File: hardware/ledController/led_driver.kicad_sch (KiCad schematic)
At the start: 1 part

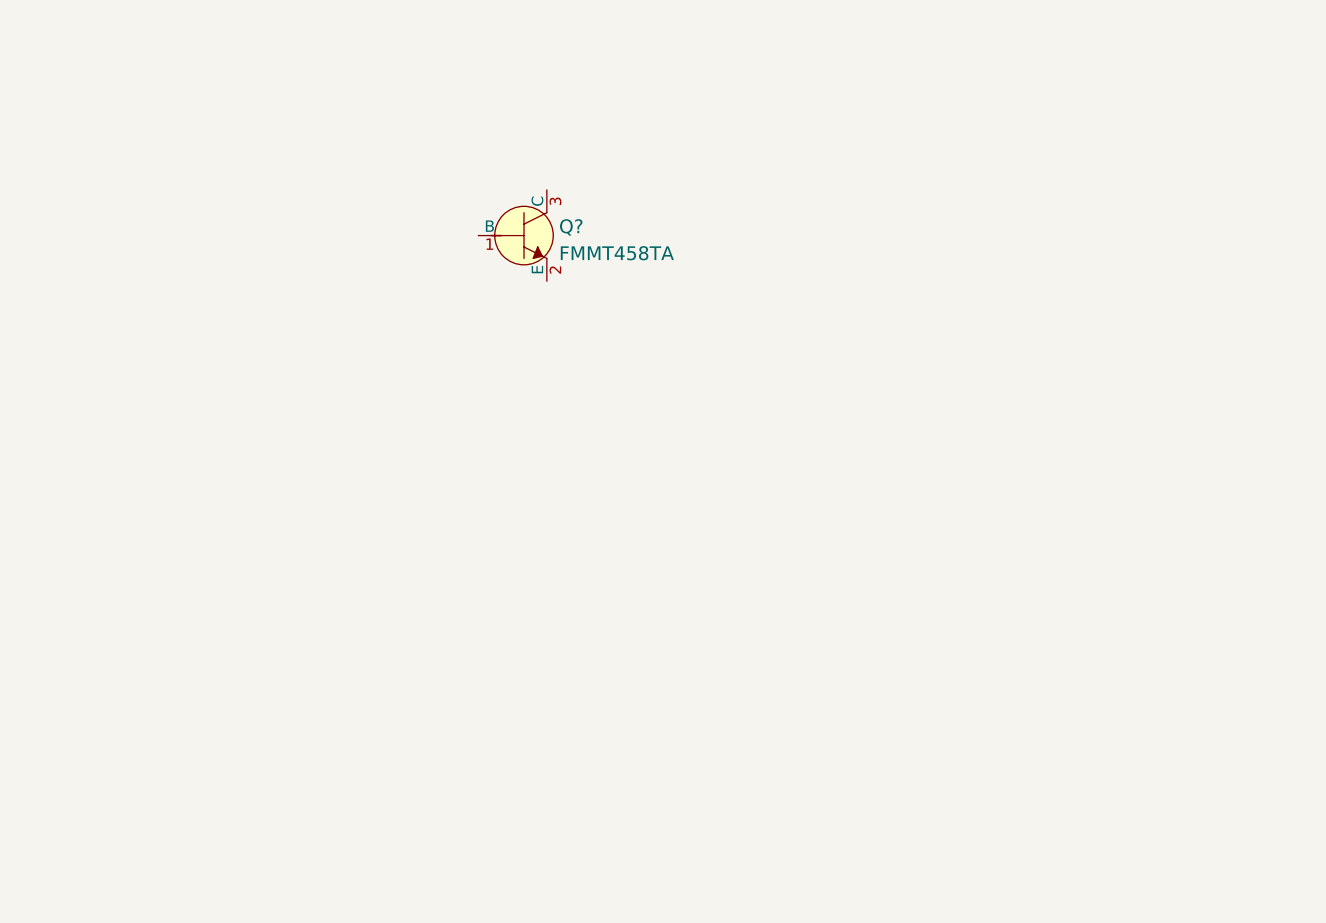
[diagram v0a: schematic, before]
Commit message: Added new schematic page for led current driver
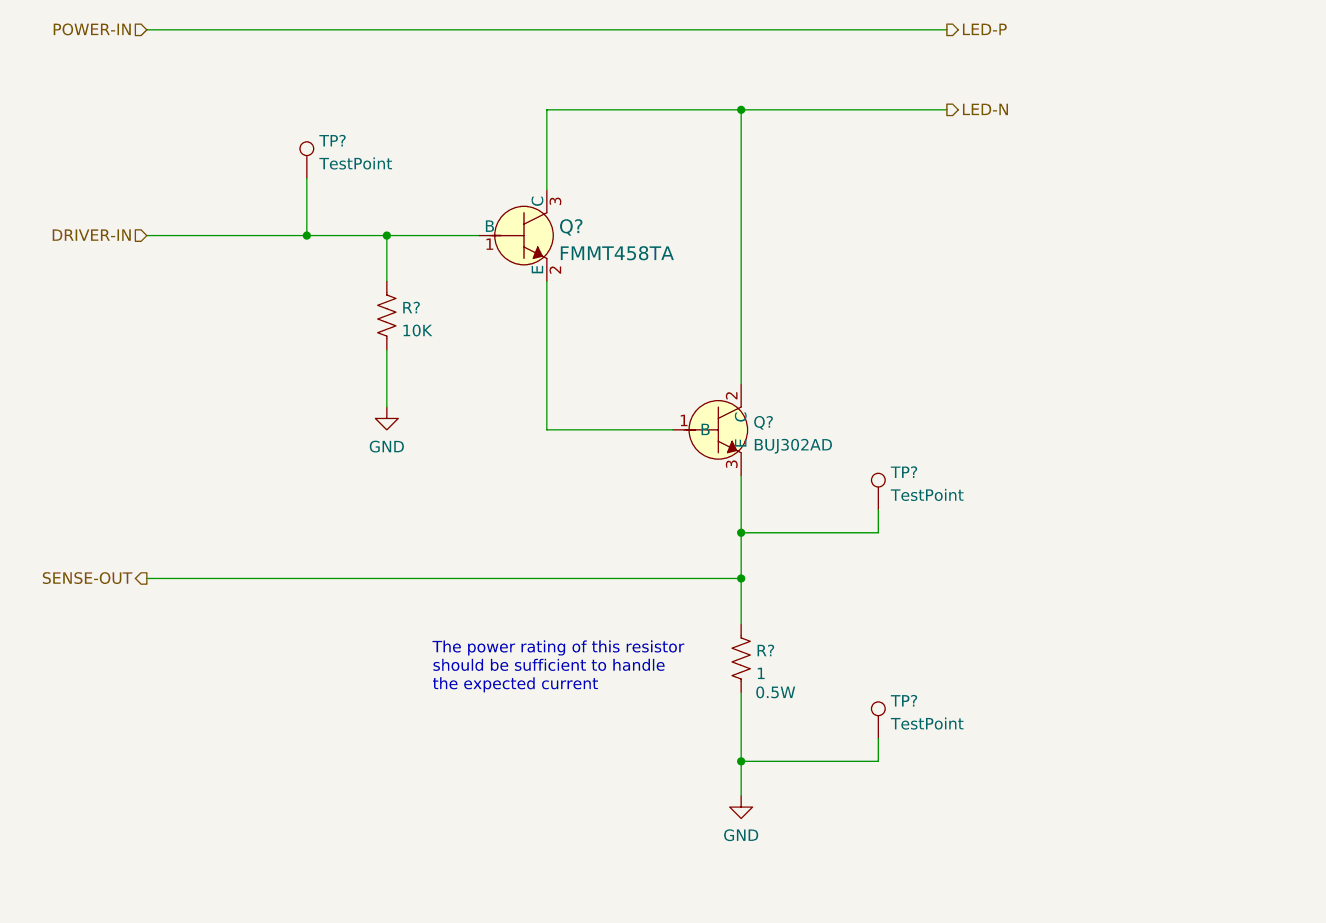
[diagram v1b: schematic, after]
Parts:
- added Q?: BUJ302AD, ym-footprints:SOT-428, symbol ym_BJT:BUJ302AD
- added R?: 10K, Resistor_SMD:R_0402_1005Metric_Pad0.72x0.64mm_HandSolder, symbol Device:R_US
- added R?: 1, Resistor_SMD:R_1210_3225Metric_Pad1.30x2.65mm_HandSolder, symbol Device:R_US
- added TP? (x3): TestPoint, TestPoint:TestPoint_Pad_D1.5mm, symbol Connector:TestPoint
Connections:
- net DRIVER-IN: now reaches Q?.1 (B)
- net DRIVER-IN: now also R?.1, TP?.1
- net at Q?.2 (E): now also Q?.1 (B)
- net LED-N: now reaches Q?.3 (C)
- net LED-N: now also Q?.2 (C)
- new net GND: R?.2, R?.2, TP?.1
- new net SENSE-OUT: Q?.3 (E), R?.1, TP?.1
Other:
- note added: "The power rating of this resistor should be sufficient to handle the expected current"
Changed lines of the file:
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@@
 (kicad_sch (version 20211123) (generator eeschema)
   (paper "A4")
+  (junction (at 102.87 72.39) (diameter 0) (color 0 0 0 0)
+  )
+  (junction (at 142.24 110.49) (diameter 0) (color 0 0 0 0)
+  )
+  (junction (at 142.24 130.81) (diameter 0) (color 0 0 0 0)
+  )
+  (junction (at 142.24 58.42) (diameter 0) (color 0 0 0 0)
+  )
+  (junction (at 93.98 72.39) (diameter 0) (color 0 0 0 0)
+  )
+  (junction (at 142.24 105.41) (diameter 0) (color 0 0 0 0)
+  )
+  (wire (pts (xy 102.87 72.39) (xy 102.87 77.47))
+    (stroke (width 0) (type default) (color 0 0 0 0))
+  )
+  (wire (pts (xy 157.48 128.27) (xy 157.48 130.81))
+    (stroke (width 0) (type default) (color 0 0 0 0))
+  )
+  (wire (pts (xy 142.24 99.06) (xy 142.24 105.41))
+    (stroke (width 0) (type default) (color 0 0 0 0))
+  )
+  (wire (pts (xy 76.2 49.53) (xy 165.1 49.53))
+    (stroke (width 0) (type default) (color 0 0 0 0))
+  )
+  (wire (pts (xy 120.65 93.98) (xy 134.62 93.98))
+    (stroke (width 0) (type default) (color 0 0 0 0))
+  )
+  (wire (pts (xy 76.2 110.49) (xy 142.24 110.49))
+    (stroke (width 0) (type default) (color 0 0 0 0))
+  )
+  (wire (pts (xy 76.2 72.39) (xy 93.98 72.39))
+    (stroke (width 0) (type default) (color 0 0 0 0))
+  )
+  (wire (pts (xy 142.24 130.81) (xy 157.48 130.81))
+    (stroke (width 0) (type default) (color 0 0 0 0))
+  )
+  (wire (pts (xy 157.48 102.87) (xy 157.48 105.41))
+    (stroke (width 0) (type default) (color 0 0 0 0))
+  )
+  (wire (pts (xy 142.24 58.42) (xy 142.24 88.9))
+    (stroke (width 0) (type default) (color 0 0 0 0))
+  )
+  (wire (pts (xy 113.03 72.39) (xy 102.87 72.39))
+    (stroke (width 0) (type default) (color 0 0 0 0))
+  )
+  (wire (pts (xy 142.24 58.42) (xy 165.1 58.42))
+    (stroke (width 0) (type default) (color 0 0 0 0))
+  )
+  (wire (pts (xy 120.65 67.31) (xy 120.65 58.42))
+    (stroke (width 0) (type default) (color 0 0 0 0))
+  )
+  (wire (pts (xy 102.87 85.09) (xy 102.87 91.44))
+    (stroke (width 0) (type default) (color 0 0 0 0))
+  )
+  (wire (pts (xy 120.65 58.42) (xy 142.24 58.42))
+    (stroke (width 0) (type default) (color 0 0 0 0))
+  )
+  (wire (pts (xy 93.98 66.04) (xy 93.98 72.39))
+    (stroke (width 0) (type default) (color 0 0 0 0))
+  )
+  (wire (pts (xy 142.24 105.41) (xy 142.24 110.49))
+    (stroke (width 0) (type default) (color 0 0 0 0))
+  )
+  (wire (pts (xy 142.24 105.41) (xy 157.48 105.41))
+    (stroke (width 0) (type default) (color 0 0 0 0))
+  )
+  (wire (pts (xy 120.65 77.47) (xy 120.65 93.98))
+    (stroke (width 0) (type default) (color 0 0 0 0))
+  )
+  (wire (pts (xy 142.24 123.19) (xy 142.24 130.81))
+    (stroke (width 0) (type default) (color 0 0 0 0))
+  )
+  (wire (pts (xy 142.24 130.81) (xy 142.24 134.62))
+    (stroke (width 0) (type default) (color 0 0 0 0))
+  )
+  (wire (pts (xy 93.98 72.39) (xy 102.87 72.39))
+    (stroke (width 0) (type default) (color 0 0 0 0))
+  )
+  (wire (pts (xy 142.24 110.49) (xy 142.24 115.57))
+    (stroke (width 0) (type default) (color 0 0 0 0))
+  )
+  (text "The power rating of this resistor\nshould be sufficient to handle\nthe expected current"
+    (at 107.95 123.19 0)
+    (effects (font (size 1.27 1.27)) (justify left bottom))
+  )
+  (hierarchical_label "SENSE-OUT" (shape output) (at 76.2 110.49 180)
+    (effects (font (size 1.27 1.27)) (justify right))
+  )
+  (hierarchical_label "LED-P" (shape output) (at 165.1 49.53 0)
+    (effects (font (size 1.27 1.27)) (justify left))
+  )
+  (hierarchical_label "POWER-IN" (shape input) (at 76.2 49.53 180)
+    (effects (font (size 1.27 1.27)) (justify right))
+  )
+  (hierarchical_label "LED-N" (shape output) (at 165.1 58.42 0)
+    (effects (font (size 1.27 1.27)) (justify left))
+  )
+  (hierarchical_label "DRIVER-IN" (shape input) (at 76.2 72.39 180)
+    (effects (font (size 1.27 1.27)) (justify right))
+  )
   (symbol (lib_id "dk_Transistors-Bipolar-BJT-Single:FMMT458TA") (at 118.11 72.39 0) (unit 1)
     (in_bom yes) (on_board yes) (fields_autoplaced)
@@
     (pin "3")
   )
+  (symbol (lib_id "Connector:TestPoint") (at 157.48 128.27 0) (unit 1)
+    (in_bom yes) (on_board yes) (fields_autoplaced)
+    (property "Reference" "TP?" (id 0) (at 158.877 124.1333 0)
+      (effects (font (size 1.27 1.27)) (justify left))
+    )
+    (property "Value" "TestPoint" (id 1) (at 158.877 126.6702 0)
+      (effects (font (size 1.27 1.27)) (justify left))
+    )
+    (property "Footprint" "TestPoint:TestPoint_Pad_D1.5mm" (id 2) (at 162.56 128.27 0)
+      (effects (font (size 1.27 1.27)) hide)
+    )
+    (property "Datasheet" "~" (id 3) (at 162.56 128.27 0)
+      (effects (font (size 1.27 1.27)) hide)
+    )
+    (pin "1")
+  )
+  (symbol (lib_id "power:GND") (at 142.24 134.62 0) (unit 1)
+    (in_bom yes) (on_board yes) (fields_autoplaced)
+    (property "Reference" "#PWR?" (id 0) (at 142.24 140.97 0)
+      (effects (font (size 1.27 1.27)) hide)
+    )
+    (property "Value" "GND" (id 1) (at 142.24 139.0634 0))
+    (property "Footprint" "" (id 2) (at 142.24 134.62 0)
+      (effects (font (size 1.27 1.27)) hide)
+    )
+    (property "Datasheet" "" (id 3) (at 142.24 134.62 0)
+      (effects (font (size 1.27 1.27)) hide)
+    )
+    (pin "1")
+  )
+  (symbol (lib_id "Connector:TestPoint") (at 93.98 66.04 0) (unit 1)
+    (in_bom yes) (on_board yes) (fields_autoplaced)
+    (property "Reference" "TP?" (id 0) (at 95.377 61.9033 0)
+      (effects (font (size 1.27 1.27)) (justify left))
+    )
+    (property "Value" "TestPoint" (id 1) (at 95.377 64.4402 0)
+      (effects (font (size 1.27 1.27)) (justify left))
+    )
+    (property "Footprint" "TestPoint:TestPoint_Pad_D1.5mm" (id 2) (at 99.06 66.04 0)
+      (effects (font (size 1.27 1.27)) hide)
+    )
+    (property "Datasheet" "~" (id 3) (at 99.06 66.04 0)
+      (effects (font (size 1.27 1.27)) hide)
+    )
+    (pin "1")
+  )
+  (symbol (lib_id "Device:R_US") (at 102.87 81.28 0) (unit 1)
+    (in_bom yes) (on_board yes) (fields_autoplaced)
+    (property "Reference" "R?" (id 0) (at 104.521 80.4453 0)
+      (effects (font (size 1.27 1.27)) (justify left))
+    )
+    (property "Value" "10K" (id 1) (at 104.521 82.9822 0)
+      (effects (font (size 1.27 1.27)) (justify left))
+    )
+    (property "Footprint" "Resistor_SMD:R_0402_1005Metric_Pad0.72x0.64mm_HandSolder" (id 2) (at 103.886 81.534 90)
+      (effects (font (size 1.27 1.27)) hide)
+    )
+    (property "Datasheet" "~" (id 3) (at 102.87 81.28 0)
+      (effects (font (size 1.27 1.27)) hide)
+    )
+    (pin "1")
+    (pin "2")
+  )
+  (symbol (lib_id "Device:R_US") (at 142.24 119.38 0) (unit 1)
+    (in_bom yes) (on_board yes)
+    (property "Reference" "R?" (id 0) (at 143.891 118.5453 0)
+      (effects (font (size 1.27 1.27)) (justify left))
+    )
+    (property "Value" "1" (id 1) (at 143.891 121.0822 0)
+      (effects (font (size 1.27 1.27)) (justify left))
+    )
+    (property "Footprint" "Resistor_SMD:R_1210_3225Metric_Pad1.30x2.65mm_HandSolder" (id 2) (at 143.256 119.634 90)
+      (effects (font (size 1.27 1.27)) hide)
+    )
+    (property "Datasheet" "~" (id 3) (at 142.24 119.38 0)
+      (effects (font (size 1.27 1.27)) hide)
+    )
+    (property "Power" "0.5W" (id 4) (at 146.05 123.19 0))
+    (pin "1")
+    (pin "2")
+  )
+  (symbol (lib_id "ym_BJT:BUJ302AD") (at 139.7 93.98 0) (unit 1)
+    (in_bom yes) (on_board yes) (fields_autoplaced)
+    (property "Reference" "Q?" (id 0) (at 143.5862 93.1453 0)
+      (effects (font (size 1.27 1.27)) (justify left))
+    )
+    (property "Value" "BUJ302AD" (id 1) (at 143.5862 95.6822 0)
+      (effects (font (size 1.27 1.27)) (justify left))
+    )
+    (property "Footprint" "ym-footprints:SOT-428" (id 2) (at 139.7 93.98 0)
+      (effects (font (size 1.27 1.27)) hide)
+    )
+    (property "Datasheet" "https://www.ween-semi.com/sites/default/files/2018-11/BUJ302AD.pdf" (id 3) (at 139.7 93.98 0)
+      (effects (font (size 1.27 1.27)) hide)
+    )
+    (pin "1")
+    (pin "2")
+    (pin "3")
+  )
+  (symbol (lib_id "Connector:TestPoint") (at 157.48 102.87 0) (unit 1)
+    (in_bom yes) (on_board yes) (fields_autoplaced)
+    (property "Reference" "TP?" (id 0) (at 158.877 98.7333 0)
+      (effects (font (size 1.27 1.27)) (justify left))
+    )
+    (property "Value" "TestPoint" (id 1) (at 158.877 101.2702 0)
+      (effects (font (size 1.27 1.27)) (justify left))
+    )
+    (property "Footprint" "TestPoint:TestPoint_Pad_D1.5mm" (id 2) (at 162.56 102.87 0)
+      (effects (font (size 1.27 1.27)) hide)
+    )
+    (property "Datasheet" "~" (id 3) (at 162.56 102.87 0)
+      (effects (font (size 1.27 1.27)) hide)
+    )
+    (pin "1")
+  )
+  (symbol (lib_id "power:GND") (at 102.87 91.44 0) (unit 1)
+    (in_bom yes) (on_board yes) (fields_autoplaced)
+    (property "Reference" "#PWR?" (id 0) (at 102.87 97.79 0)
+      (effects (font (size 1.27 1.27)) hide)
+    )
+    (property "Value" "GND" (id 1) (at 102.87 95.8834 0))
+    (property "Footprint" "" (id 2) (at 102.87 91.44 0)
+      (effects (font (size 1.27 1.27)) hide)
+    )
+    (property "Datasheet" "" (id 3) (at 102.87 91.44 0)
+      (effects (font (size 1.27 1.27)) hide)
+    )
+    (pin "1")
+  )
 )

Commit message: Added BJT base resistor and some cleanup
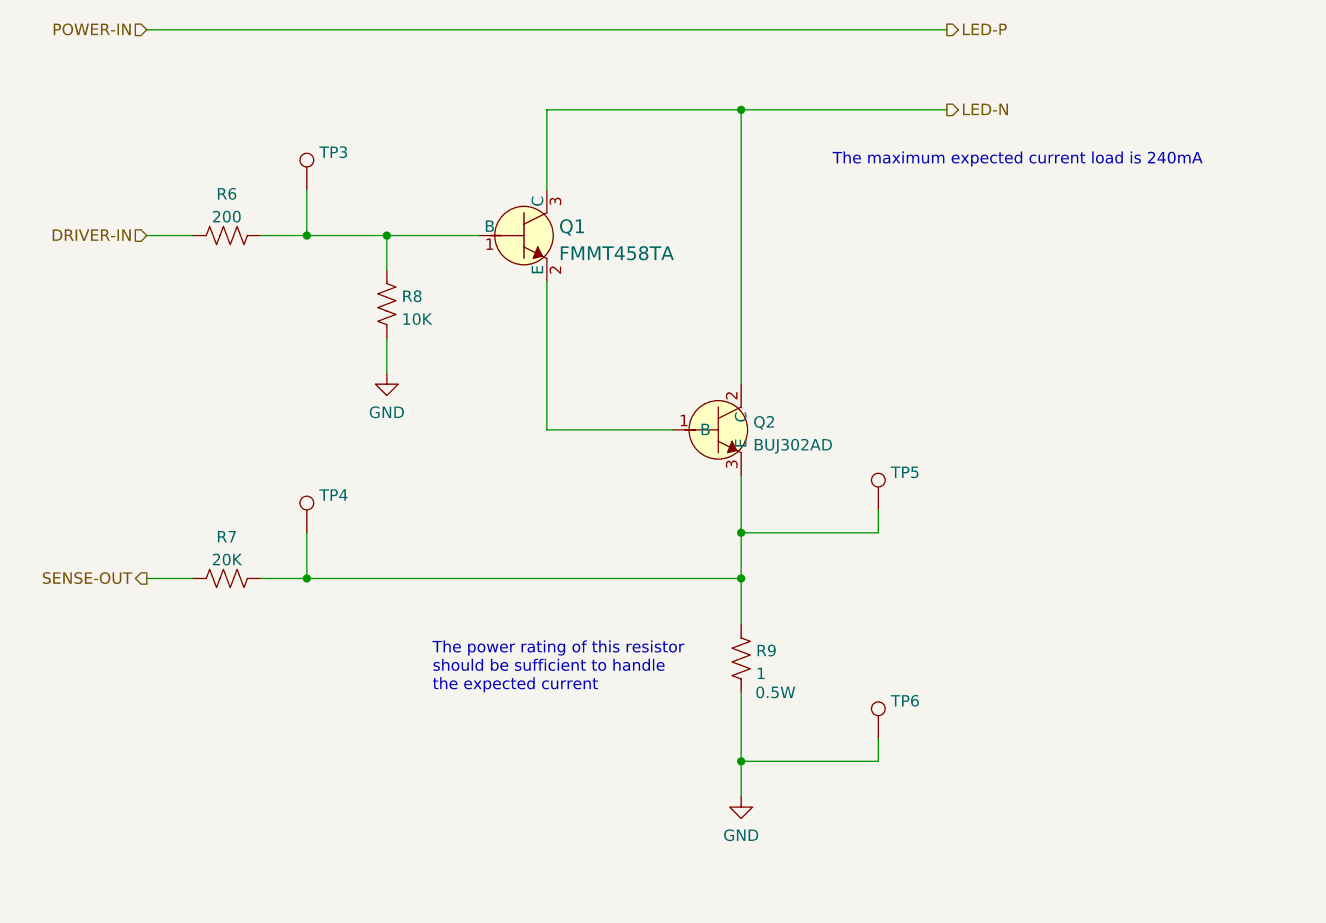
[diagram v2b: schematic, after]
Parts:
- added R6: 200, Resistor_SMD:R_0603_1608Metric_Pad0.98x0.95mm_HandSolder, symbol Device:R_US
- added R7: 20K, Resistor_SMD:R_0603_1608Metric_Pad0.98x0.95mm_HandSolder, symbol Device:R_US
- added TP4: TestPoint, TestPoint:TestPoint_Pad_D1.5mm, symbol Connector:TestPoint
- R8: renamed from R?; footprint Resistor_SMD:R_0402_1005Metric_Pad0.72x0.64mm_HandSolder -> Resistor_SMD:R_0603_1608Metric_Pad0.98x0.95mm_HandSolder
- gave numbers to parts that had none: 6
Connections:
- net DRIVER-IN: now also R6.1; no longer Q1.1 (B), R8.1, TP3.1
- net SENSE-OUT: now also R7.1; no longer Q2.3 (E), R9.1, TP5.1
- new net: Q1.1 (B), R6.2, R8.1, TP3.1
- new net: Q2.3 (E), R7.2, R9.1, TP4.1, TP5.1
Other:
- note added: "The maximum expected current load is 240mA"
- title: (none) -> Lantern
- moved on the sheet: R8, TP3
